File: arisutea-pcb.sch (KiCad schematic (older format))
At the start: 54 parts, among them J12 VCC, J13 D+, J14 D-, J15 GND, J16 RGB, J17 RGB_IN, J18 RGB_OUT, J2 MISO, J3 +5V, J4 SCK, J5 MOSI, J6 ~RES~, J7 GND, U1 USBLC6-2SC6, U2 ATmega32U4-AU, Y1 Crystal_GND24

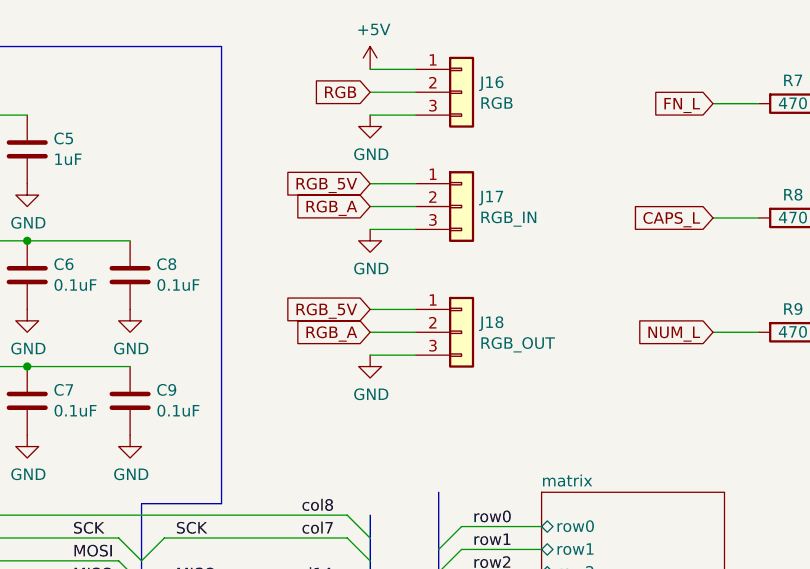
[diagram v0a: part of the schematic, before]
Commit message: WS2812 PADS ADDED
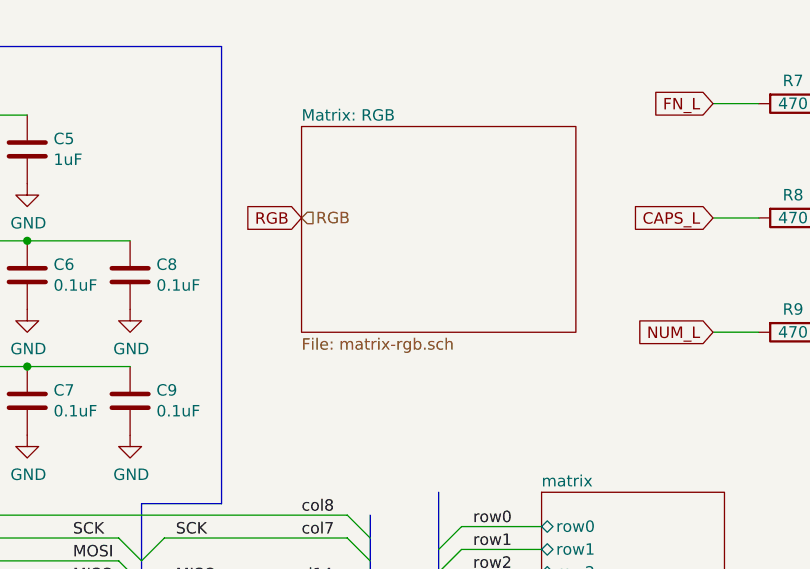
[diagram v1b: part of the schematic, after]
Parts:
- removed J16: RGB, arisutea:PinHeader_1x03_P2.54mm_Vertical, symbol Connector_Generic:Conn_01x03
- removed J17: RGB_IN, arisutea:PinHeader_1x03_P2.54mm_Vertical, symbol Connector_Generic:Conn_01x03
- removed J18: RGB_OUT, arisutea:PinHeader_1x03_P2.54mm_Vertical, symbol Connector_Generic:Conn_01x03
- LOGO5: footprint arisutea:arisutea_logo -> arisutea:QMK_Logo_Dark
- LOGO6: value arisutea_logo -> QMK_LOGO; footprint arisutea:arisutea_logo -> arisutea:QMK_Logo_Dark
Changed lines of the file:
@@
 $Descr A4 11693 8268
 encoding utf-8
-Sheet 1 2
+Sheet 1 3
 Title "Arisutea Keyboard"
 Date "2021-03-27"
@@
 	1    0    0    -1
 $EndComp
-$Comp
-L Connector_Generic:Conn_01x03 J16
-U 1 1 605F9602
-P 7600 900
-F 0 "J16" H 7680 942 50  0000 L CNN
-F 1 "RGB" H 7680 851 50  0000 L CNN
-F 2 "arisutea:PinHeader_1x03_P2.54mm_Vertical" H 7600 900 50  0001 C CNN
-F 3 "~" H 7600 900 50  0001 C CNN
-	1    7600 900
-	1    0    0    -1
-$EndComp
-Text GLabel 7200 900  0    50   Input ~ 0
+Text GLabel 6900 1450 0    50   Input ~ 0
 RGB
-$Comp
-L power:+5V #PWR0124
-U 1 1 605FC221
-P 7200 800
-F 0 "#PWR0124" H 7200 650 50  0001 C CNN
-F 1 "+5V" H 7215 973 50  0000 C CNN
-F 2 "" H 7200 800 50  0001 C CNN
-F 3 "" H 7200 800 50  0001 C CNN
-	1    7200 800
-	1    0    0    -1
-$EndComp
-$Comp
-L power:GND #PWR0125
-U 1 1 605FDE52
-P 7200 1000
-F 0 "#PWR0125" H 7200 750 50  0001 C CNN
-F 1 "GND" H 7205 827 50  0000 C CNN
-F 2 "" H 7200 1000 50  0001 C CNN
-F 3 "" H 7200 1000 50  0001 C CNN
-	1    7200 1000
-	1    0    0    -1
-$EndComp
-Wire Wire Line
-	7200 800  7400 800
-Wire Wire Line
-	7200 1000 7400 1000
-$Comp
-L Connector_Generic:Conn_01x03 J17
-U 1 1 60611535
-P 7600 1400
-F 0 "J17" H 7680 1442 50  0000 L CNN
-F 1 "RGB_IN" H 7680 1351 50  0000 L CNN
-F 2 "arisutea:PinHeader_1x03_P2.54mm_Vertical" H 7600 1400 50  0001 C CNN
-F 3 "~" H 7600 1400 50  0001 C CNN
-	1    7600 1400
-	1    0    0    -1
-$EndComp
-Text GLabel 7200 1400 0    50   Input ~ 0
-RGB_A
-$Comp
-L power:GND #PWR0127
-U 1 1 6061154A
-P 7200 1500
-F 0 "#PWR0127" H 7200 1250 50  0001 C CNN
-F 1 "GND" H 7205 1327 50  0000 C CNN
-F 2 "" H 7200 1500 50  0001 C CNN
-F 3 "" H 7200 1500 50  0001 C CNN
-	1    7200 1500
-	1    0    0    -1
-$EndComp
-Wire Wire Line
-	7200 1300 7400 1300
-Wire Wire Line
-	7200 1500 7400 1500
-$Comp
-L Connector_Generic:Conn_01x03 J18
-U 1 1 6062103D
-P 7600 1950
-F 0 "J18" H 7680 1992 50  0000 L CNN
-F 1 "RGB_OUT" H 7680 1901 50  0000 L CNN
-F 2 "arisutea:PinHeader_1x03_P2.54mm_Vertical" H 7600 1950 50  0001 C CNN
-F 3 "~" H 7600 1950 50  0001 C CNN
-	1    7600 1950
-	1    0    0    -1
-$EndComp
-Text GLabel 7200 1950 0    50   Input ~ 0
-RGB_A
-$Comp
-L power:GND #PWR0129
-U 1 1 60621052
-P 7200 2050
-F 0 "#PWR0129" H 7200 1800 50  0001 C CNN
-F 1 "GND" H 7205 1877 50  0000 C CNN
-F 2 "" H 7200 2050 50  0001 C CNN
-F 3 "" H 7200 2050 50  0001 C CNN
-	1    7200 2050
-	1    0    0    -1
-$EndComp
-Wire Wire Line
-	7200 1850 7400 1850
-Wire Wire Line
-	7200 2050 7400 2050
-Text GLabel 7200 1300 0    50   Input ~ 0
-RGB_5V
-Text GLabel 7200 1850 0    50   Input ~ 0
-RGB_5V
-Wire Wire Line
-	7200 900  7400 900
-Wire Wire Line
-	7200 1400 7400 1400
-Wire Wire Line
-	7200 1950 7400 1950
 Text GLabel 6400 6900 2    50   Input ~ 0
 RGB
@@
 F 0 "LOGO5" H 10100 6300 50  0000 C CNN
 F 1 "arisutea_logo" H 10175 6474 50  0001 C CNN
-F 2 "arisutea:arisutea_logo" H 10100 6450 50  0001 C CNN
+F 2 "arisutea:QMK_Logo_Dark" H 10100 6450 50  0001 C CNN
 F 3 "" H 10100 6450 50  0001 C CNN
 	1    10100 6100
@@
 P 10450 6100
 F 0 "LOGO6" H 10450 6300 50  0000 C CNN
-F 1 "arisutea_logo" H 10525 6474 50  0001 C CNN
-F 2 "arisutea:arisutea_logo" H 10450 6450 50  0001 C CNN
+F 1 "QMK_LOGO" H 10525 6474 50  0001 C CNN
+F 2 "arisutea:QMK_Logo_Dark" H 10450 6450 50  0001 C CNN
 F 3 "" H 10450 6450 50  0001 C CNN
 	1    10450 6100
 	1    0    0    -1
 $EndComp
+$Sheet
+S 6900 1050 1200 900
+U 6063AA46
+F0 "Matrix: RGB" 50
+F1 "matrix-rgb.sch" 50
+$EndSheet
+Text HLabel 6900 1450 2    50   Input ~ 0
+RGB
 Wire Bus Line
 	6200 2700 6200 3150
